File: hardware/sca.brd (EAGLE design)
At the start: 99 x 73.3 mm, 31 parts

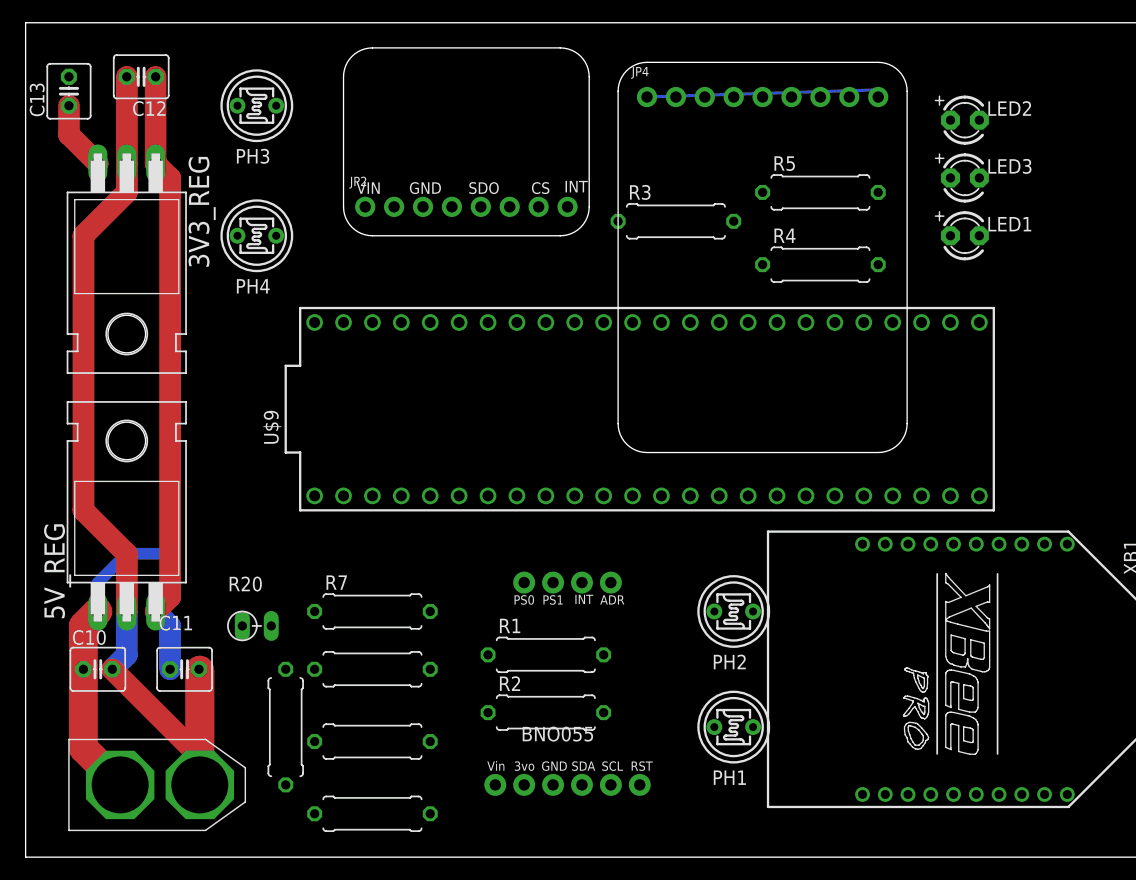
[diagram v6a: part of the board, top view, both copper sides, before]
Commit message: initial routing / changed xbee tx/rx for routing reasons
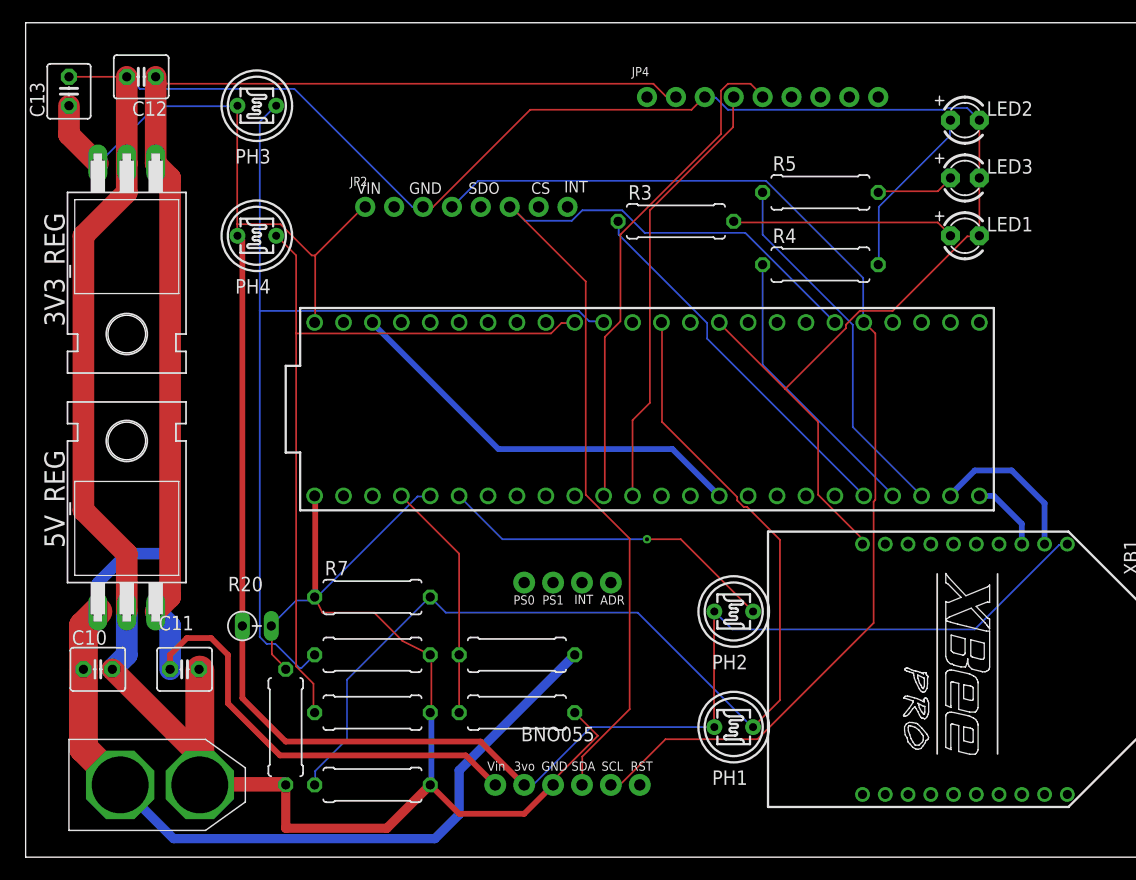
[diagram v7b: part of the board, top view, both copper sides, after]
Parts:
- moved R6 2.54 mm to (30.5, 6.35)
- moved R1 2.54 mm to (43.2, 17.8)
- moved R2 2.54 mm to (43.2, 12.7)
- moved R9 2.54 mm to (30.5, 12.7)
- moved R7 1.27 mm to (30.5, 22.9)
- moved R8 1.27 mm to (30.5, 17.8)
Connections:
- removed net MCU_RX: U$9.0, XB1.2
- removed net MCU_TX: U$9.1, XB1.3
- new net XBEE_RX: U$9.32/A13, XB1.3
- new net XBEE_TX: U$9.31/A12, XB1.2
- net PR_2: now also U$9.4; no longer U$9.15/A1
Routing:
- net GND: track 79.3 -> 307.1 mm
- net +3V3: track 6.13 -> 184.6 mm
- net SCL: track 0.00 -> 100.4 mm
- net SDA: track 0.00 -> 90.5 mm
- net +5V: track 53.6 -> 138.2 mm
- net PR_3: track 0.00 -> 84.4 mm
- net PR_1: track 0.00 -> 74.1 mm
- net PR_4: track 0.00 -> 68.2 mm
- net V_BATT: track 27.0 -> 77.9 mm
- net PR_2: track 0.00 -> 50.3 mm, vias 0 -> 1
- net GPS_TX: track 0.00 -> 44.3 mm
- net GPS_RX: track 0.00 -> 38.7 mm
- net 3.3V: track 0.00 -> 36.8 mm
- net LED_1: track 0.00 -> 33.1 mm
- net LED_3: track 0.00 -> 32.5 mm
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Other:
- outline, holes or cut-outs redrawn

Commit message: routing...
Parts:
- moved R7 5.08 mm to (30.5, 17.8)
- moved R8 5.08 mm to (30.5, 22.9)
- moved R10 1.27 mm to (21.6, 11.4)
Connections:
- net PR_4: now also U$9.0; no longer U$9.17/A3
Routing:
- net PR_4: track 68.2 -> 49.6 mm
- net PR_2: track 50.3 -> 60.7 mm
- net GND: track 307.1 -> 315.5 mm
- net PR_3: track 84.4 -> 76.1 mm
- net +3V3: track 184.6 -> 189.7 mm
- net PR_1: track 74.1 -> 75.1 mm
